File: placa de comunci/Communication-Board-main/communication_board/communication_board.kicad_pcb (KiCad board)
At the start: 2 copper layers, 103 x 100 mm, 66 parts, among them J1 USB_IN, J10 B4B-XH-A, J11 B4B-XH-A, J12 XT60-M, J13 B4B-XH-A, J14 B4B-XH-A, J15 B4B-XH-A, J16 B4B-XH-A, J17 B4B-XH-A, J2 IMU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

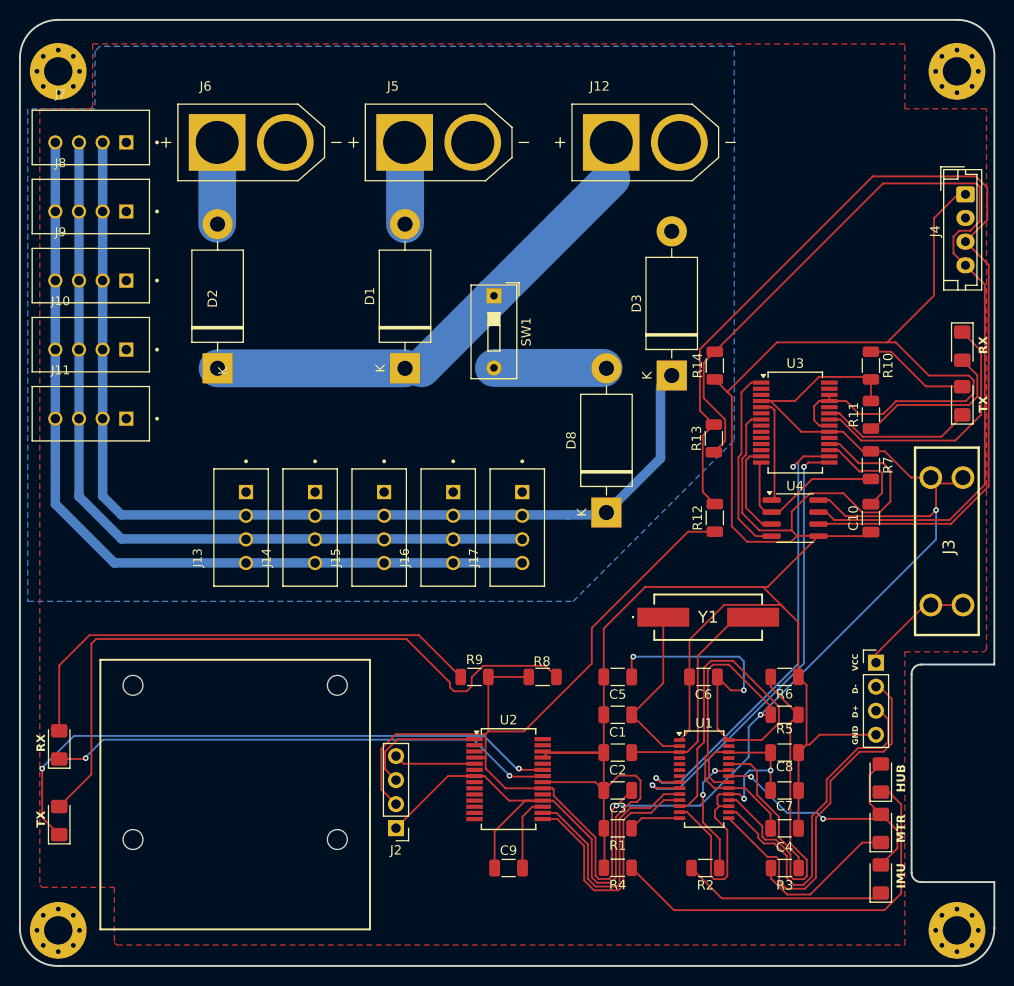
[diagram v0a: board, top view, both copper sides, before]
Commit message: imu nova (MPU6050)
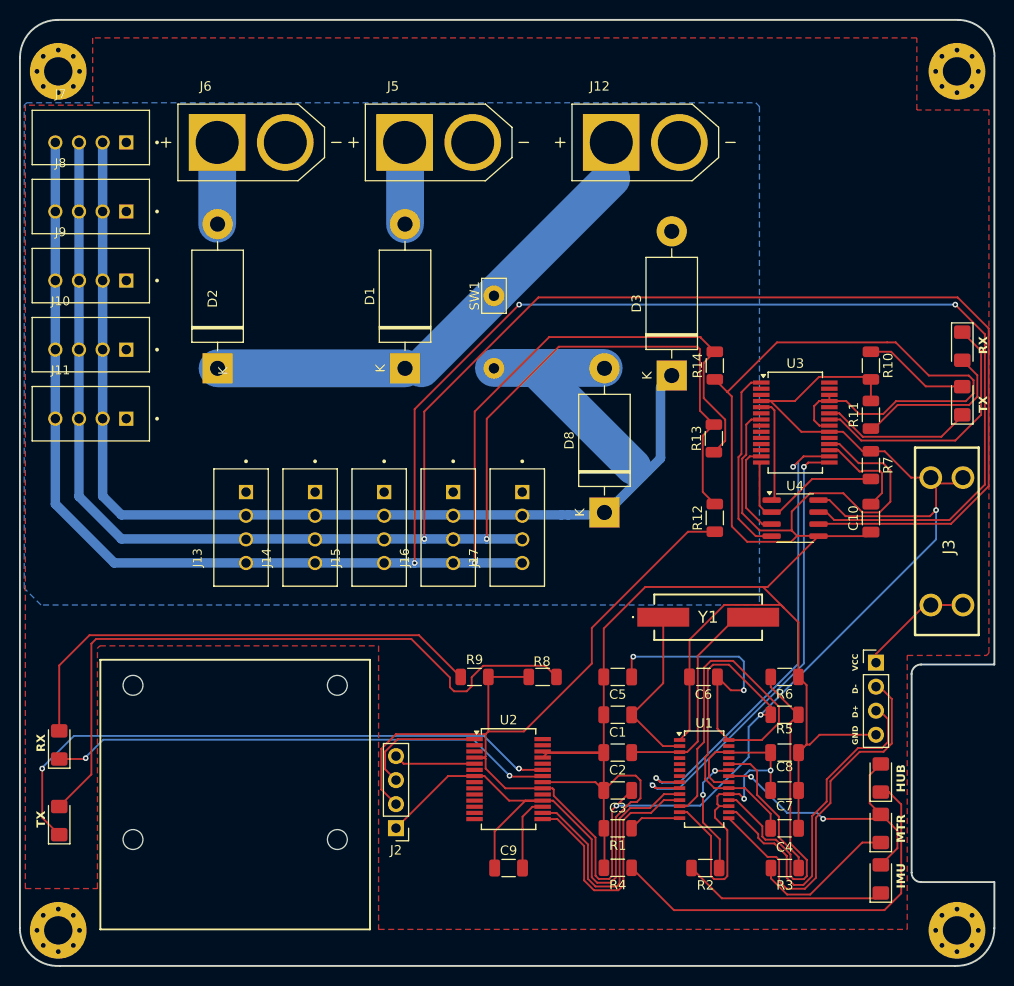
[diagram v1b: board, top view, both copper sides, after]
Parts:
- removed J4: Motors, Connector_JST:JST_EH_B4B-EH-A_1x04_P2.50mm_Vertical
- added ?: , , F.Cu at (149.4, 59.7)
- SW1: footprint Button_Switch_THT:SW_DIP_SPSTx01_Slide_9.78x4.72mm_W7.62mm_P2.54mm -> Connector_Pin:Pin_D1.1mm_L10.2mm_W3.5mm_Flat
- moved D8 0.21 mm to (161.0, 74.9)
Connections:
- J10 pad 1: GND -> GNDREF
- J11 pad 1: GND -> GNDREF
- J12 pad N: GND -> GNDREF
- J13 pad 1: GND -> GNDREF
- J14 pad 1: GND -> GNDREF
- J15 pad 1: GND -> GNDREF
- J16 pad 1: GND -> GNDREF
- J17 pad 1: GND -> GNDREF
- J5 pad N: GND -> GNDREF
- J6 pad N: GND -> GNDREF
- J7 pad 1: GND -> GNDREF
- J8 pad 1: GND -> GNDREF
- J9 pad 1: GND -> GNDREF
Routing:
- net Net-(U4-B): track 102.2 -> 265.9 mm, vias 0 -> 4
- net Net-(U4-A): track 109.6 -> 258.5 mm, vias 0 -> 2
- net Net-(D1-K): track 53.7 -> 191.1 mm
- net Net-(D3-K): track 109.0 -> 0.00 mm
- net Net-(J10-Pad4): track 90.2 -> 0.00 mm
- net Net-(J10-Pad3): track 86.2 -> 0.00 mm
- net GNDREF: track 339.6 -> 320.1 mm
- net Net-(D8-A): track 12.1 -> 0.00 mm
- added copper zone on B.Cu, net GNDREF
- removed copper zone on B.Cu, net GND
